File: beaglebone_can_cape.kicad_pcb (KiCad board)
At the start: 2 copper layers, 86.4 x 54.6 mm, 24 parts, among them J1 DCAN0, J2 DCAN1, P8 BeagleBone_Black_Header, P9 BeagleBone_Black_Header, U1 TCAN332, U2 TCAN332, U3 LMR51430

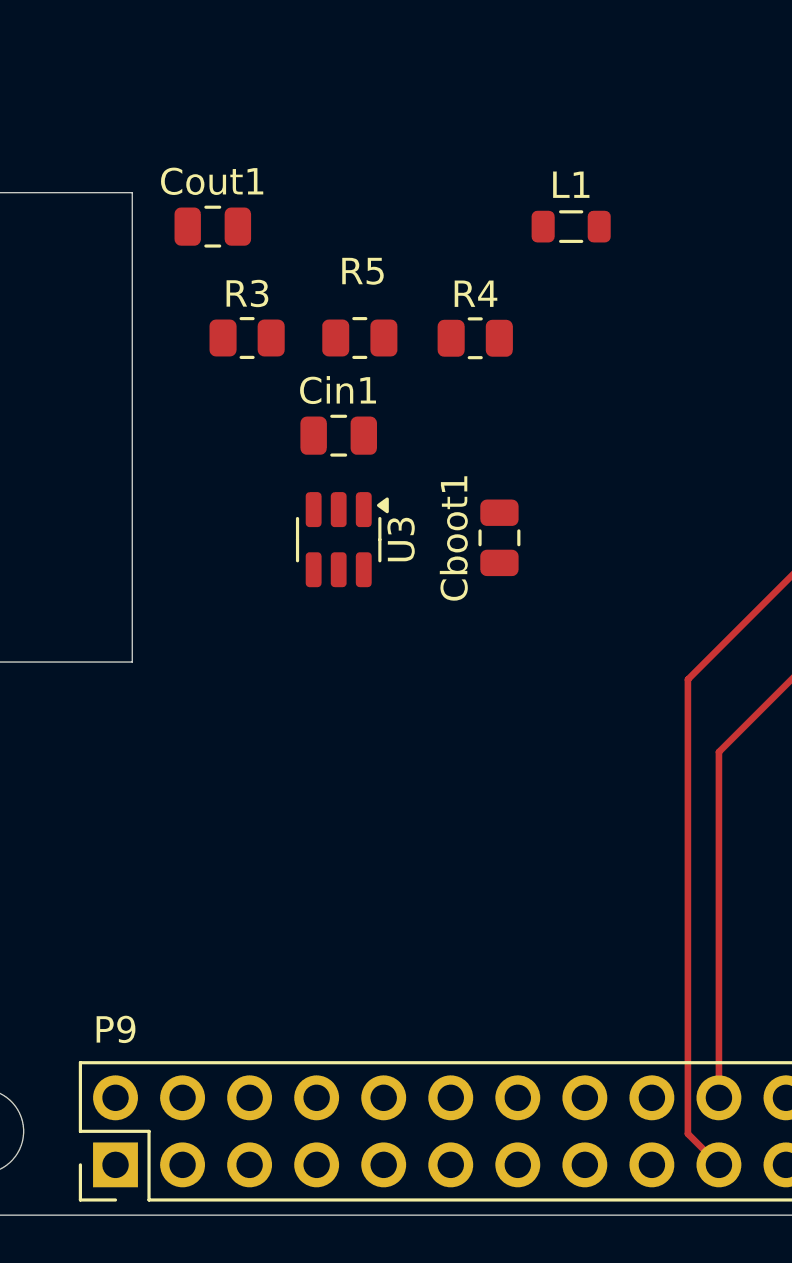
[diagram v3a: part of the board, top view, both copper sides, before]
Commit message: Symbol may not be needed, we will see...
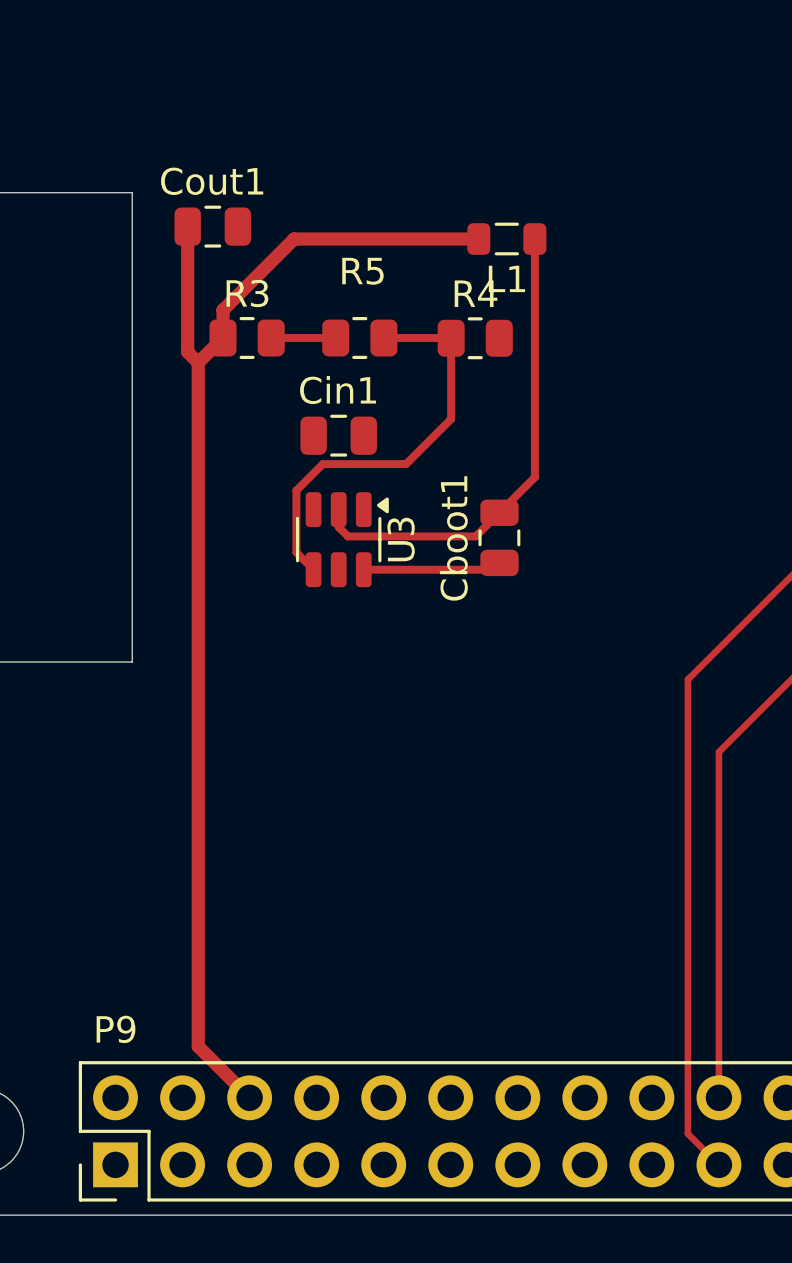
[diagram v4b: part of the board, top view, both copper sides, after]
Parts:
- moved L1 2.48 mm to (134.5, 63.0), turned to 180 degrees
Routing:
- net +5V: track 0.00 -> 47.2 mm
- net Net-(U3-SW): track 0.00 -> 18.2 mm
- net Net-(U3-FB): track 0.00 -> 15.9 mm
- net Net-(U3-CB): track 0.00 -> 5.25 mm
- net Net-(R3-Pad2): track 0.00 -> 2.45 mm
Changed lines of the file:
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@@
 	(footprint "Inductor_SMD:L_0805_2012Metric"
 		(layer "F.Cu")
-		(at 136.9475 62.55)
+		(at 134.51 63.02 180)
 		(descr "Inductor SMD 0805 (2012 Metric), square (rectangular) end terminal, IPC-7351 nominal, (Body size source: IPC-SM-782 page 80, https://www.pcb-3d.com/wordpress/wp-content/uploads/ipc-sm-782a_amendment_1_and_2.pdf), generated with kicad-footprint-generator")
 		(tags "inductor")
@@
 		(attr smd)
 		(fp_line
-			(start -0.399622 -0.56)
-			(end 0.399622 -0.56)
+			(start -0.399622 0.56)
+			(end 0.399622 0.56)
 			(stroke
 				(width 0.12)
@@
 		)
 		(fp_line
-			(start -0.399622 0.56)
-			(end 0.399622 0.56)
+			(start -0.399622 -0.56)
+			(end 0.399622 -0.56)
 			(stroke
 				(width 0.12)
@@
 		)
 		(fp_line
-			(start -1.75 -0.85)
-			(end 1.75 -0.85)
+			(start 1.75 0.85)
+			(end -1.75 0.85)
 			(stroke
 				(width 0.05)
@@
 		)
 		(fp_line
-			(start -1.75 0.85)
-			(end -1.75 -0.85)
+			(start 1.75 -0.85)
+			(end 1.75 0.85)
 			(stroke
 				(width 0.05)
@@
 		)
 		(fp_line
-			(start 1.75 -0.85)
-			(end 1.75 0.85)
+			(start -1.75 0.85)
+			(end -1.75 -0.85)
 			(stroke
 				(width 0.05)
@@
 		)
 		(fp_line
-			(start 1.75 0.85)
-			(end -1.75 0.85)
+			(start -1.75 -0.85)
+			(end 1.75 -0.85)
 			(stroke
 				(width 0.05)
@@
 		)
 		(fp_line
-			(start -1 -0.45)
-			(end 1 -0.45)
+			(start 1 0.45)
+			(end -1 0.45)
 			(stroke
 				(width 0.1)
@@
 		)
 		(fp_line
-			(start -1 0.45)
-			(end -1 -0.45)
+			(start 1 -0.45)
+			(end 1 0.45)
 			(stroke
 				(width 0.1)
@@
 		)
 		(fp_line
-			(start 1 -0.45)
-			(end 1 0.45)
+			(start -1 0.45)
+			(end -1 -0.45)
 			(stroke
 				(width 0.1)
@@
 		)
 		(fp_line
-			(start 1 0.45)
-			(end -1 0.45)
+			(start -1 -0.45)
+			(end 1 -0.45)
 			(stroke
 				(width 0.1)
@@
 		)
 		(pad "1" smd roundrect
-			(at -1.0625 0)
+			(at -1.0625 0 180)
 			(size 0.875 1.2)
 			(layers "F.Cu" "F.Mask" "F.Paste")
@@
 		)
 		(pad "2" smd roundrect
-			(at 1.0625 0)
+			(at 1.0625 0 180)
 			(size 0.875 1.2)
 			(layers "F.Cu" "F.Mask" "F.Paste")
@@
 	)
 	(segment
+		(start 123.7575 66.77)
+		(end 123.7575 65.7125)
+		(width 0.5)
+		(layer "F.Cu")
+		(net 52)
+	)
+	(segment
+		(start 123.7575 65.7125)
+		(end 126.45 63.02)
+		(width 0.5)
+		(layer "F.Cu")
+		(net 52)
+	)
+	(segment
+		(start 122.82 67.7075)
+		(end 122.42 67.3075)
+		(width 0.5)
+		(layer "F.Cu")
+		(net 52)
+	)
+	(segment
+		(start 124.765 95.555)
+		(end 122.82 93.61)
+		(width 0.5)
+		(layer "F.Cu")
+		(net 52)
+	)
+	(segment
+		(start 122.42 67.3075)
+		(end 122.42 62.55)
+		(width 0.5)
+		(layer "F.Cu")
+		(net 52)
+	)
+	(segment
+		(start 126.45 63.02)
+		(end 133.4475 63.02)
+		(width 0.5)
+		(layer "F.Cu")
+		(net 52)
+	)
+	(segment
+		(start 122.82 67.7075)
+		(end 123.7575 66.77)
+		(width 0.5)
+		(layer "F.Cu")
+		(net 52)
+	)
+	(segment
+		(start 122.82 93.61)
+		(end 122.82 67.7075)
+		(width 0.5)
+		(layer "F.Cu")
+		(net 52)
+	)
+	(segment
 		(start 153.424999 89.755001)
 		(end 147.625 95.555)
@@
 		(net 89)
 	)
+	(segment
+		(start 133.334 74.286)
+		(end 128.491001 74.286)
+		(width 0.3)
+		(layer "F.Cu")
+		(net 91)
+	)
+	(segment
+		(start 135.5725 72.0475)
+		(end 134.23 73.39)
+		(width 0.3)
+		(layer "F.Cu")
+		(net 91)
+	)
+	(segment
+		(start 128.14 73.934999)
+		(end 128.14 73.2725)
+		(width 0.3)
+		(layer "F.Cu")
+		(net 91)
+	)
+	(segment
+		(start 134.23 73.39)
+		(end 133.334 74.286)
+		(width 0.3)
+		(layer "F.Cu")
+		(net 91)
+	)
+	(segment
+		(start 135.5725 63.02)
+		(end 135.5725 72.0475)
+		(width 0.3)
+		(layer "F.Cu")
+		(net 91)
+	)
+	(segment
+		(start 128.491001 74.286)
+		(end 128.14 73.934999)
+		(width 0.3)
+		(layer "F.Cu")
+		(net 91)
+	)
+	(segment
+		(start 133.9725 75.5475)
+		(end 134.23 75.29)
+		(width 0.3)
+		(layer "F.Cu")
+		(net 92)
+	)
+	(segment
+		(start 129.09 75.5475)
+		(end 133.9725 75.5475)
+		(width 0.3)
+		(layer "F.Cu")
+		(net 92)
+	)
+	(segment
+		(start 125.5825 66.77)
+		(end 128.0275 66.77)
+		(width 0.3)
+		(layer "F.Cu")
+		(net 94)
+	)
+	(segment
+		(start 130.694 71.546)
+		(end 132.4 69.84)
+		(width 0.3)
+		(layer "F.Cu")
+		(net 95)
+	)
+	(segment
+		(start 126.539 72.548322)
+		(end 127.541322 71.546)
+		(width 0.3)
+		(layer "F.Cu")
+		(net 95)
+	)
+	(segment
+		(start 127.19 75.5475)
+		(end 126.539 74.8965)
+		(width 0.3)
+		(layer "F.Cu")
+		(net 95)
+	)
+	(segment
+		(start 127.541322 71.546)
+		(end 130.694 71.546)
+		(width 0.3)
+		(layer "F.Cu")
+		(net 95)
+	)
+	(segment
+		(start 129.8525 66.77)
+		(end 132.39 66.77)
+		(width 0.3)
+		(layer "F.Cu")
+		(net 95)
+	)
+	(segment
+		(start 132.39 66.77)
+		(end 132.4 66.78)
+		(width 0.3)
+		(layer "F.Cu")
+		(net 95)
+	)
+	(segment
+		(start 126.539 74.8965)
+		(end 126.539 72.548322)
+		(width 0.3)
+		(layer "F.Cu")
+		(net 95)
+	)
+	(segment
+		(start 132.4 69.84)
+		(end 132.4 66.78)
+		(width 0.3)
+		(layer "F.Cu")
+		(net 95)
+	)
 	(zone

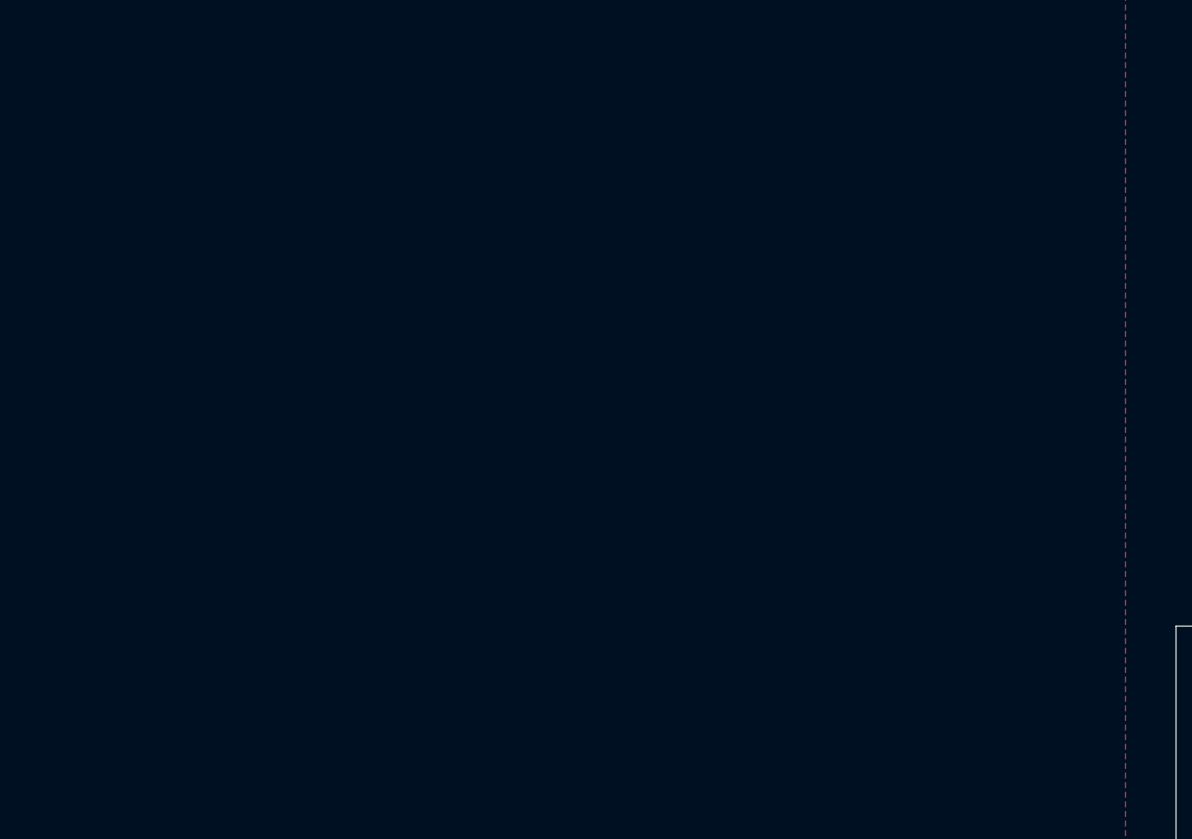
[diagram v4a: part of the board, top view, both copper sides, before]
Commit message: Schematic + PCB support of Deutsch
* Imported the DTM15-12PA footprint (this one is not correct as Marlin has a smaller footprint I know now)
* Removed "PWR" label and replaced with 5V net
* Reviewed the new schematic fooprint that Zach added, looks good
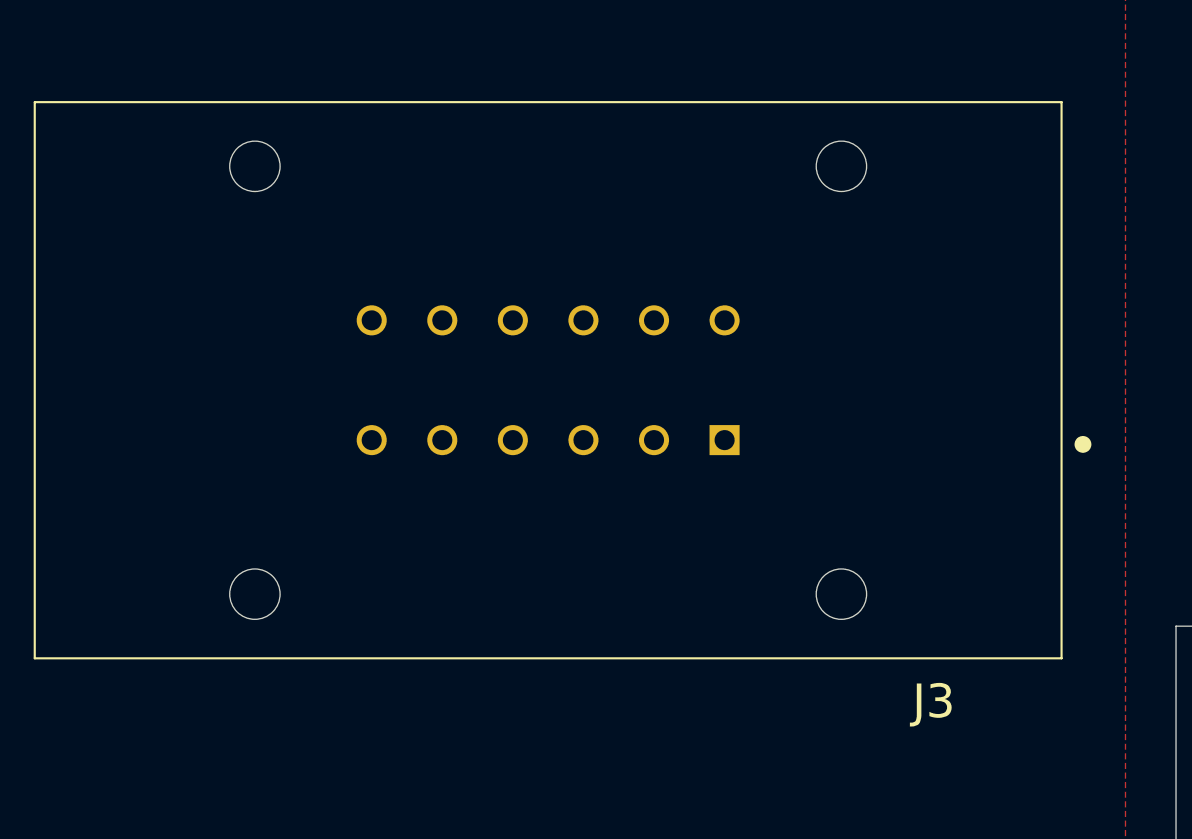
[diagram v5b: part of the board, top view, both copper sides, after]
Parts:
- added J3: DTM15-12PA, Senior Design:TE_DTM15-12PA, F.Cu at (62.7, 64.4)
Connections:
- net Net-(J2-Pin_1) renamed CAN LOW 1
- net Net-(J2-Pin_2) renamed CAN HIGH 1
- Cout1 pad 1: +5V -> Net-(Cout1-Pad1)
- L1 pad 2: +5V -> Net-(Cout1-Pad1)
- P9 pad 5: +5V -> PWR
- R3 pad 1: +5V -> Net-(Cout1-Pad1)

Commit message: taking break, letting Nash cook
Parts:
- removed J3: DTM15-12PA, Senior Design:TE_DTM15-12PA
- added J4: Conn_02x02_Top_Bottom, Connector_PinHeader_2.54mm:PinHeader_2x02_P2.54mm_Vertical, F.Cu at (89.2, 83.7)
- added J5: Battery Harness, SeniorDesign:BatteryHolder, F.Cu at (87.1, 65.3)
- added R6: 10k, Resistor_SMD:R_0805_2012Metric, F.Cu at (86.4, 70.2)
- added SW1: SW_Push, SeniorDesign:SKQYAAE010, F.Cu at (79.5, 75.6)
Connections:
- Cout1 pad 1: Net-(Cout1-Pad1) -> PWR
- L1 pad 2: Net-(Cout1-Pad1) -> PWR
- R3 pad 1: Net-(Cout1-Pad1) -> PWR
